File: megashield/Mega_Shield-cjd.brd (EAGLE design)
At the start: 101.6 x 53.3 mm, 17 parts

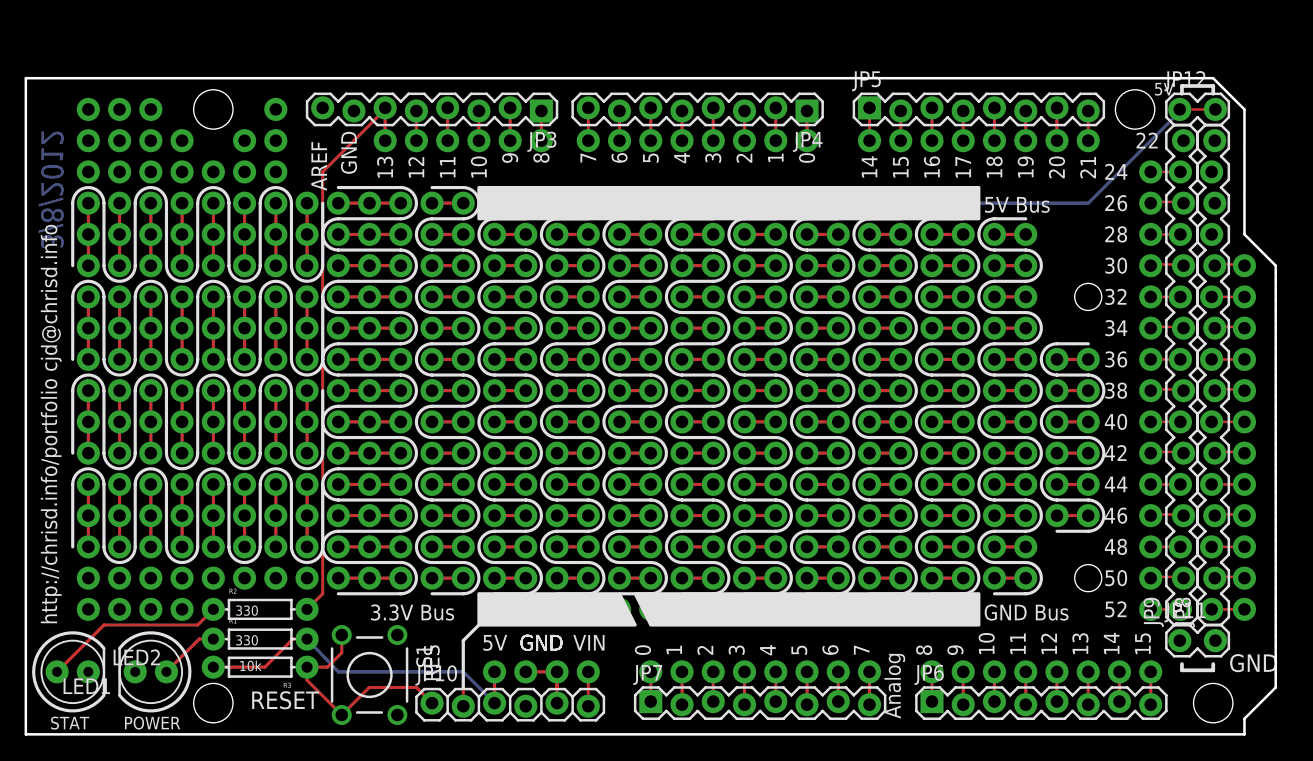
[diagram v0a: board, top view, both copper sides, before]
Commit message: Update with larger busses
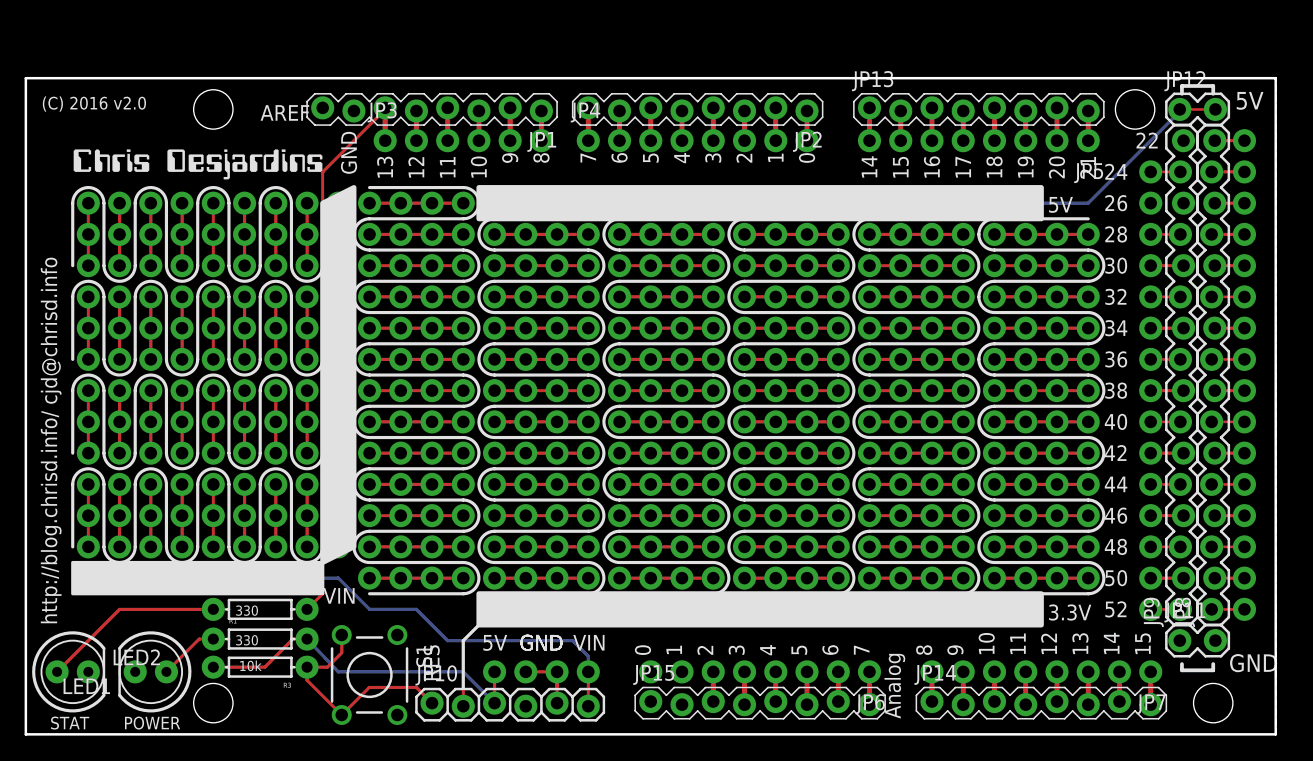
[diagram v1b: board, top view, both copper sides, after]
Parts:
- added JP1, JP13, JP14, JP15, JP2: (no value), SparkFun-Connectors:1X08_LOCK_NO_PIN1
- added U$1: (no value), desjardins:LOGO
- JP3: device SparkFun:1X08_LOCK -> SparkFun-Connectors:1X06_NO_SILK
- JP4, JP5, JP6, JP7: device SparkFun:1X08_LOCK -> SparkFun-Connectors:1X08_NO_SILK
- moved JP7 40.7 mm to (91.4, 5.08), turned to 180 degrees
- moved JP4 18.0 mm to (45.7, 48.3), turned to 0 degrees
- moved JP5 18.0 mm to (86.4, 48.3), turned to 180 degrees
- moved JP3 13.0 mm to (29.2, 48.3), turned to 0 degrees
- moved JP6 5.68 mm to (68.6, 5.08), turned to 180 degrees
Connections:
- net A0: now also JP15.1, JP6.8; no longer JP7.1
- net A1: now also JP15.2, JP6.7; no longer JP7.2
- net A10: now also JP14.3, JP7.6; no longer JP6.3
- net A11: now also JP14.4, JP7.5; no longer JP6.4
- net A12: now also JP14.5, JP7.4; no longer JP6.5
- net A13: now also JP14.6, JP7.3; no longer JP6.6
- net A14: now also JP14.7, JP7.2; no longer JP6.7
- net A15: now also JP14.8, JP7.1; no longer JP6.8
- net A2: now also JP15.3, JP6.6; no longer JP7.3
- net A3: now also JP15.4, JP6.5; no longer JP7.4
- net A4: now also JP15.5, JP6.4; no longer JP7.5
- net A5: now also JP15.6, JP6.3; no longer JP7.6
- net A6: now also JP15.7, JP6.2; no longer JP7.7
- net A7: now also JP15.8, JP6.1; no longer JP7.8
- net A8: now also JP14.1, JP7.8; no longer JP6.1
- net A9: now also JP14.2, JP7.7; no longer JP6.2
- net AREF: now also JP1.8; no longer JP3.8
- net D10: now also JP1.3, JP3.4; no longer JP3.3
- net D11: now also JP1.4, JP3.3; no longer JP3.4
- net D12: now also JP1.5, JP3.2; no longer JP3.5
- net D13: now also JP1.6, JP3.1; no longer JP3.6
- net D14: now also JP13.8, JP5.1; no longer JP5.8
- net D15: now also JP13.7, JP5.2; no longer JP5.7
- net D16: now also JP13.6, JP5.3; no longer JP5.6
- net D17: now also JP13.5, JP5.4; no longer JP5.5
- net D18: now also JP13.4, JP5.5; no longer JP5.4
- net D19: now also JP13.3, JP5.6; no longer JP5.3
- net D2: now also JP2.3, JP4.6; no longer JP4.3
- net D3: now also JP2.4, JP4.5; no longer JP4.4
- net D4: now also JP2.5, JP4.4; no longer JP4.5
- net D5: now also JP2.6, JP4.3; no longer JP4.6
- net D6: now also JP2.7, JP4.2; no longer JP4.7
- net D7: now also JP2.8, JP4.1; no longer JP4.8
- net D8: now also JP1.1, JP3.6; no longer JP3.1
- net D9: now also JP1.2, JP3.5; no longer JP3.2
- net GND: now also JP1.7; no longer JP3.7
- net RX0: now also JP2.1, JP4.8; no longer JP4.1
- net SCL: now also JP13.1, JP5.8; no longer JP5.1
- net SDA: now also JP13.2, JP5.7; no longer JP5.2
- net TX1: now also JP2.2, JP4.7; no longer JP4.2
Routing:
- net VIN: track 2.79 -> 47.3 mm, vias 1 -> 9
- net N$68: track 0.00 -> 7.62 mm, vias 0 -> 4
- net N$65: track 0.00 -> 7.62 mm, vias 0 -> 4
- net N$61: track 0.00 -> 7.62 mm, vias 0 -> 4
- net N$99: track 2.54 -> 7.62 mm, vias 2 -> 4
- net N$98: track 2.54 -> 7.62 mm, vias 2 -> 4
- net N$97: track 2.54 -> 7.62 mm, vias 2 -> 4
- net N$96: track 2.54 -> 7.62 mm, vias 2 -> 4
- net N$95: track 2.54 -> 7.62 mm, vias 2 -> 4
- net N$94: track 2.54 -> 7.62 mm, vias 2 -> 4
- net N$93: track 2.54 -> 7.62 mm, vias 2 -> 4
- net N$92: track 2.54 -> 7.62 mm, vias 2 -> 4
- net N$91: track 2.54 -> 7.62 mm, vias 2 -> 4
- net N$90: track 2.54 -> 7.62 mm, vias 2 -> 4
- net N$89: track 2.54 -> 7.62 mm, vias 2 -> 4
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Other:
- outline, holes or cut-outs redrawn
- board text added: "(C) 2016 v2.0"
- board text added: "3.3V"
- board text added: "http://blog.chrisd.info/ cjd@chrisd.info"
- board text removed: "3.3V Bus"
- board text removed: "3/8/2012"
- board text removed: "5V Bus"
- board text removed: "GND Bus"
- board text removed: "RESET"
- board text removed: "http://chrisd.info/portfolio cjd@chrisd.info"

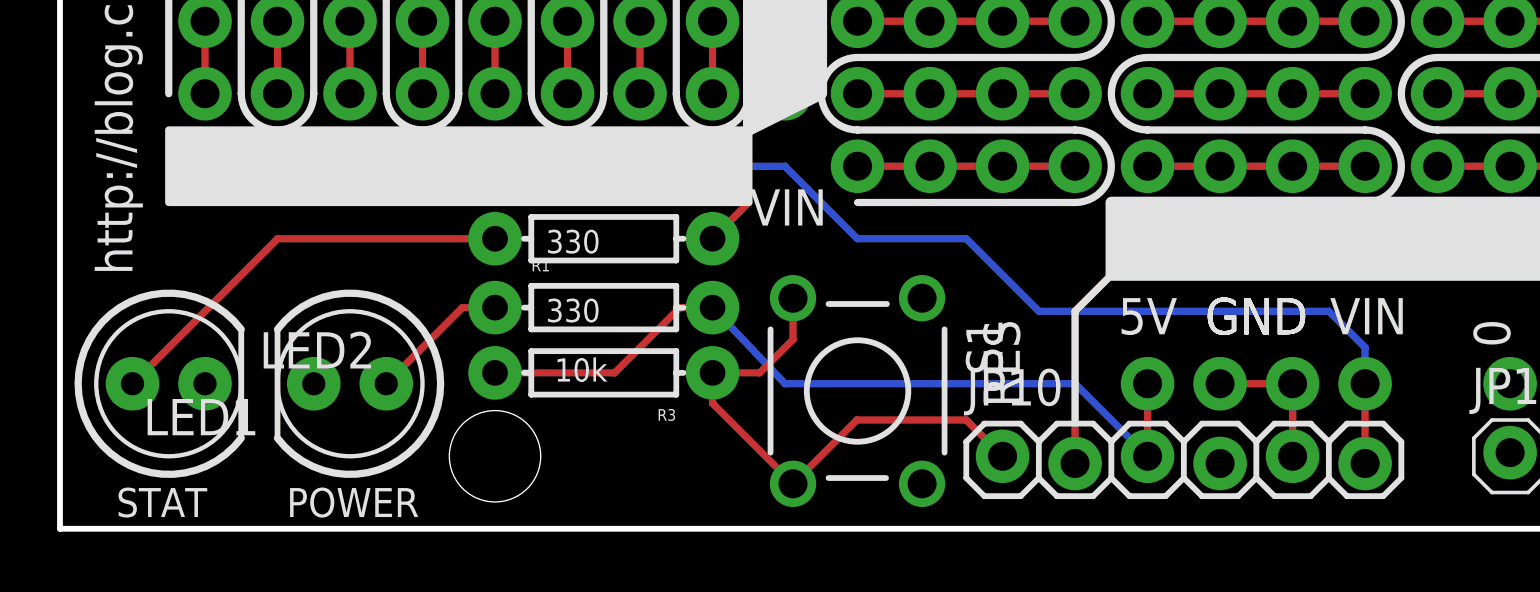
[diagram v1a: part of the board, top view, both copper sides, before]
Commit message: Add silkscreen to the bottom
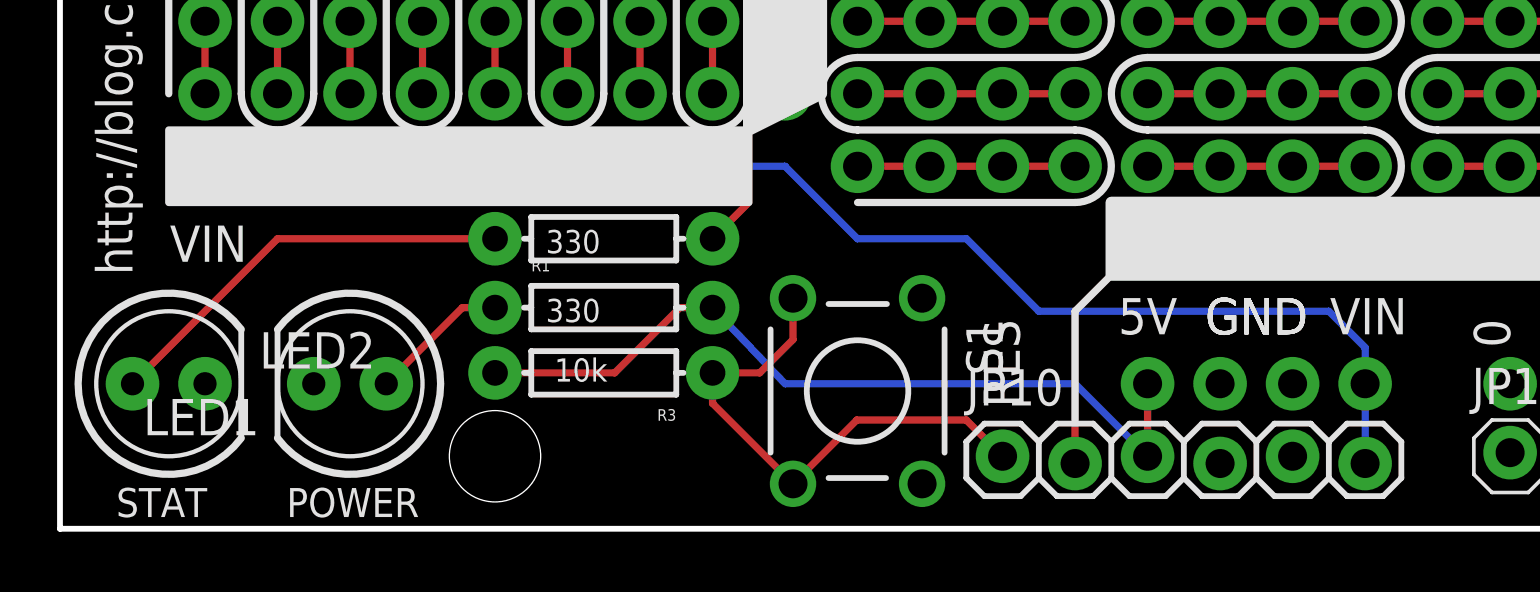
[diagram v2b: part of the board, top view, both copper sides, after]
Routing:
- net GND: track 6.35 -> 0.00 mm

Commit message: Add OSHW logo
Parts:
- added U$3: (no value), bfl:OSHW2
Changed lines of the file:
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@@
 </element>
 <element name="U$1" library="desjardins" package="LOGO" value="" x="3.81" y="45.72"/>
+<element name="U$3" library="bfl" package="OSHW2" value="" x="10.16" y="44.45" rot="MR0"/>
 </elements>
 <signals>
